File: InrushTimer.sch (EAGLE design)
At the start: 71 parts, among them IC1 TLC272D, IC2 555, IC3 4076N, Q2 TRANSISTOR-FET_2N7002, Q3 TRANSISTOR-FET_2N7002, Q4 TRANSISTOR-FET_2N7002, Q5 TRANSISTOR-FET_2N7002, Q6 DIODES_ZTX451DIODES_ZTX451_0_0, T1 MMBTA05, U1 ROHM_BY_ELEMENT14_BATCH_1_BU4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

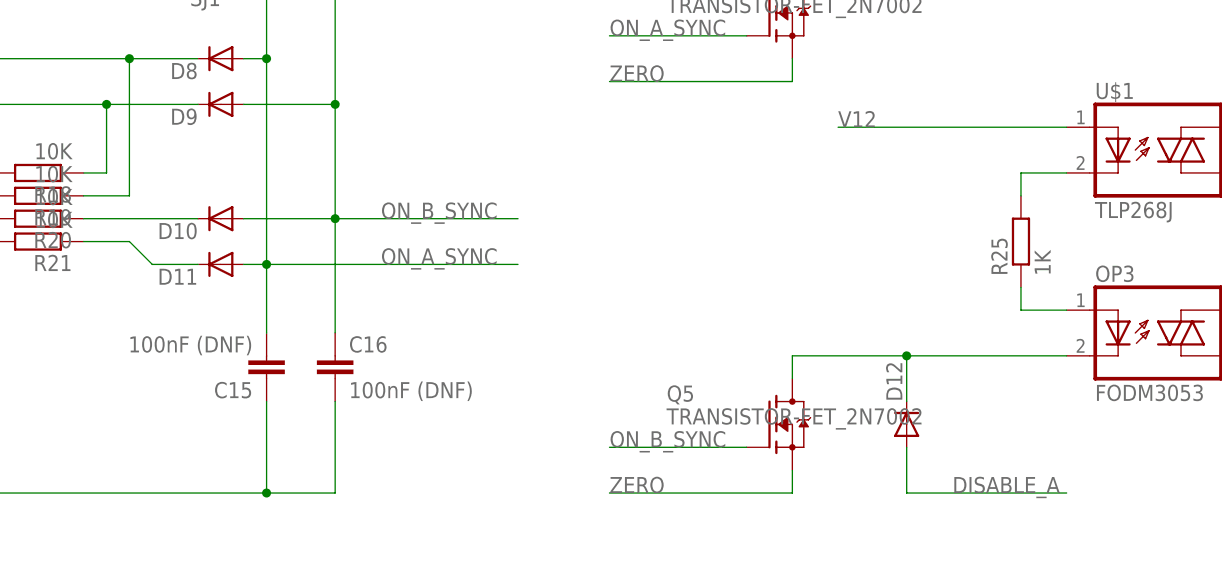
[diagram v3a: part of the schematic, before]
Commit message: Pushed some tracks to the bottom side
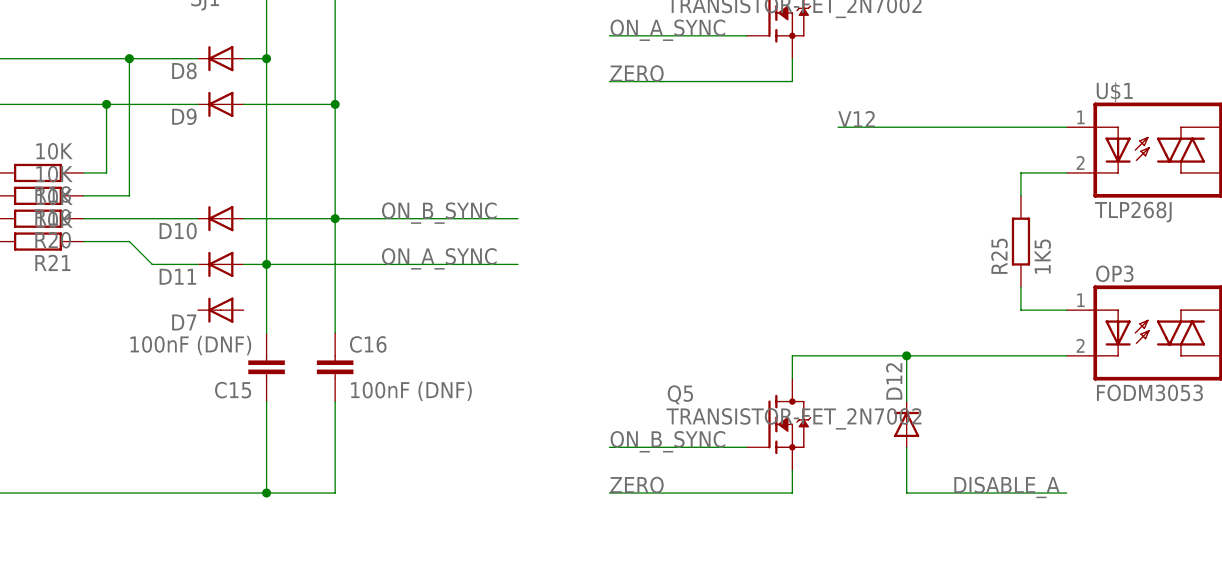
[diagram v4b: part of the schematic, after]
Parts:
- added D7: (no value), diode:DIODE-SOD323-R
- R25: value 1K -> 1K5
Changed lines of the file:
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@@
 <grid distance="0.1" unitdist="inch" unit="inch" style="lines" multiple="1" display="no" altdistance="0.01" altunitdist="inch" altunit="inch"/>
 <layers>
-<layer number="1" name="Top" color="4" fill="1" visible="no" active="no"/>
-<layer number="2" name="Route2" color="1" fill="3" visible="no" active="no"/>
-<layer number="3" name="Route3" color="4" fill="3" visible="no" active="no"/>
-<layer number="14" name="Route14" color="1" fill="6" visible="no" active="no"/>
-<layer number="15" name="Route15" color="4" fill="6" visible="no" active="no"/>
-<layer number="16" name="Bottom" color="1" fill="1" visible="no" active="no"/>
-<layer number="17" name="Pads" color="2" fill="1" visible="no" active="no"/>
-<layer number="18" name="Vias" color="2" fill="1" visible="no" active="no"/>
-<layer number="19" name="Unrouted" color="6" fill="1" visible="no" active="no"/>
-<layer number="20" name="Dimension" color="24" fill="1" visible="no" active="no"/>
-<layer number="21" name="tPlace" color="15" fill="1" visible="no" active="no"/>
-<layer number="22" name="bPlace" color="14" fill="1" visible="no" active="no"/>
-<layer number="23" name="tOrigins" color="15" fill="1" visible="no" active="no"/>
-<layer number="24" name="bOrigins" color="15" fill="1" visible="no" active="no"/>
-<layer number="25" name="tNames" color="7" fill="1" visible="no" active="no"/>
-<layer number="26" name="bNames" color="7" fill="1" visible="no" active="no"/>
-<layer number="27" name="tValues" color="7" fill="1" visible="no" active="no"/>
-<layer number="28" name="bValues" color="7" fill="1" visible="no" active="no"/>
+<layer number="1" name="Top" color="4" fill="1" visible="yes" active="no"/>
+<layer number="2" name="Route2" color="1" fill="3" visible="yes" active="no"/>
+<layer number="3" name="Route3" color="4" fill="3" visible="yes" active="no"/>
+<layer number="14" name="Route14" color="1" fill="6" visible="yes" active="no"/>
+<layer number="15" name="Route15" color="4" fill="6" visible="yes" active="no"/>
+<layer number="16" name="Bottom" color="1" fill="1" visible="yes" active="no"/>
+<layer number="17" name="Pads" color="2" fill="1" visible="yes" active="no"/>
+<layer number="18" name="Vias" color="2" fill="1" visible="yes" active="no"/>
+<layer number="19" name="Unrouted" color="6" fill="1" visible="yes" active="no"/>
+<layer number="20" name="Dimension" color="24" fill="1" visible="yes" active="no"/>
+<layer number="21" name="tPlace" color="15" fill="1" visible="yes" active="no"/>
+<layer number="22" name="bPlace" color="14" fill="1" visible="yes" active="no"/>
+<layer number="23" name="tOrigins" color="15" fill="1" visible="yes" active="no"/>
+<layer number="24" name="bOrigins" color="15" fill="1" visible="yes" active="no"/>
+<layer number="25" name="tNames" color="7" fill="1" visible="yes" active="no"/>
+<layer number="26" name="bNames" color="7" fill="1" visible="yes" active="no"/>
+<layer number="27" name="tValues" color="7" fill="1" visible="yes" active="no"/>
+<layer number="28" name="bValues" color="7" fill="1" visible="yes" active="no"/>
 <layer number="29" name="tStop" color="7" fill="3" visible="no" active="no"/>
 <layer number="30" name="bStop" color="7" fill="6" visible="no" active="no"/>
@@
 <layer number="35" name="tGlue" color="7" fill="4" visible="no" active="no"/>
 <layer number="36" name="bGlue" color="7" fill="5" visible="no" active="no"/>
-<layer number="37" name="tTest" color="7" fill="1" visible="no" active="no"/>
-<layer number="38" name="bTest" color="7" fill="1" visible="no" active="no"/>
+<layer number="37" name="tTest" color="7" fill="1" visible="yes" active="no"/>
+<layer number="38" name="bTest" color="7" fill="1" visible="yes" active="no"/>
 <layer number="39" name="tKeepout" color="4" fill="11" visible="no" active="no"/>
 <layer number="40" name="bKeepout" color="1" fill="11" visible="no" active="no"/>
@@
 <layer number="44" name="Drills" color="7" fill="1" visible="no" active="no"/>
 <layer number="45" name="Holes" color="7" fill="1" visible="no" active="no"/>
-<layer number="46" name="Milling" color="3" fill="1" visible="no" active="no"/>
-<layer number="47" name="Measures" color="7" fill="1" visible="no" active="no"/>
-<layer number="48" name="Document" color="7" fill="1" visible="no" active="no"/>
-<layer number="49" name="Reference" color="7" fill="1" visible="no" active="no"/>
-<layer number="50" name="dxf" color="7" fill="1" visible="no" active="no"/>
-<layer number="51" name="tDocu" color="6" fill="1" visible="no" active="no"/>
-<layer number="52" name="bDocu" color="7" fill="1" visible="no" active="no"/>
-<layer number="53" name="tGND_GNDA" color="7" fill="9" visible="no" active="no"/>
-<layer number="54" name="bGND_GNDA" color="1" fill="9" visible="no" active="no"/>
-<layer number="56" name="wert" color="7" fill="1" visible="no" active="no"/>
+<layer number="46" name="Milling" color="3" fill="1" visible="yes" active="no"/>
+<layer number="47" name="Measures" color="7" fill="1" visible="yes" active="no"/>
+<layer number="48" name="Document" color="7" fill="1" visible="yes" active="no"/>
+<layer number="49" name="Reference" color="7" fill="1" visible="yes" active="no"/>
+<layer number="50" name="dxf" color="7" fill="1" visible="yes" active="no"/>
+<layer number="51" name="tDocu" color="6" fill="1" visible="yes" active="no"/>
+<layer number="52" name="bDocu" color="7" fill="1" visible="yes" active="no"/>
+<layer number="53" name="tGND_GNDA" color="7" fill="9" visible="yes" active="no"/>
+<layer number="54" name="bGND_GNDA" color="1" fill="9" visible="yes" active="no"/>
+<layer number="56" name="wert" color="7" fill="1" visible="yes" active="no"/>
 <layer number="90" name="Modules" color="5" fill="1" visible="yes" active="yes"/>
 <layer number="91" name="Nets" color="2" fill="1" visible="yes" active="yes"/>
@@
 <part name="C2" library="rcl" deviceset="C-EU" device="050-024X044" value="100nF"/>
 <part name="C9" library="rcl" deviceset="C-EU" device="C1206K" value="100nF"/>
-<part name="R25" library="rcl" deviceset="R-EU_" device="0207/2V" value="1K"/>
+<part name="R25" library="rcl" deviceset="R-EU_" device="0207/2V" value="1K5"/>
 <part name="X2" library="con-wago-500" deviceset="W237-102" device=""/>
 <part name="C5" library="rcl" deviceset="C-EU" device="C0805K" value="10nF"/>
@@
 <part name="D3" library="diode" deviceset="DIODE-" device="DO34-7" value="5082-2800"/>
 <part name="U$1" library="SHoleLib" deviceset="TLP268J" device=""/>
+<part name="D7" library="diode" deviceset="DIODE-" device="SOD323-R"/>
 </parts>
 <sheets>
@@
 <instance part="D3" gate="G$1" x="-22.86" y="60.96" rot="R270"/>
 <instance part="U$1" gate="G$1" x="368.3" y="7.62"/>
+<instance part="D7" gate="G$1" x="264.16" y="-10.16" rot="R180"/>
 </instances>
 <busses>

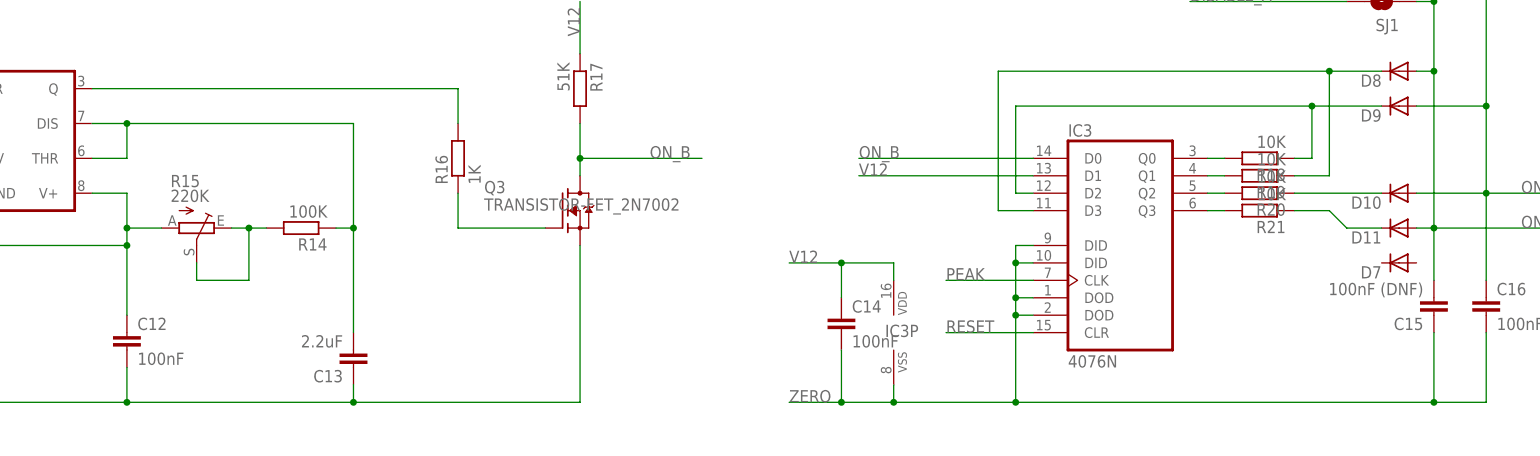
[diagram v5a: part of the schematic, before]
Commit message: Tidied up component and track placement.
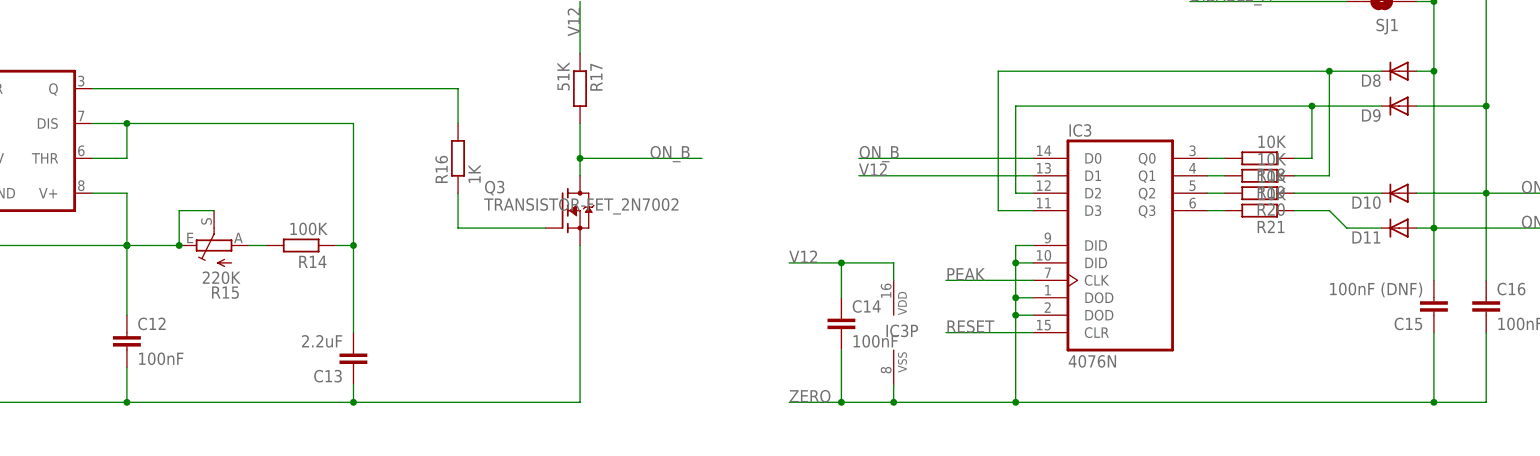
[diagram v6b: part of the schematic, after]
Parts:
- removed D7: (no value), diode:DIODE-SOD323-R
- R6: device rcl:R-EU_0207/2V -> rcl:R-EU_0207/7
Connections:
- removed net N$2: R14.2, R15.E, R15.S
- new net N$34: R14.2, R15.A
- net V12: now also R15.E, R15.S; no longer R15.A
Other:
- moved on the sheet: R14, R15
